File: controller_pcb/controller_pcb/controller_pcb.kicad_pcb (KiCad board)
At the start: 2 copper layers, 34 parts, among them J1 USB_B_Micro, Y1 8MHz

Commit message: initial wiring done
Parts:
- moved C6 3.09 mm to (144.8, 119.9)
- moved C3 2.54 mm to (159.3, 119.4)
- moved C4 2.54 mm to (166.1, 119.4)
- moved C5 2.54 mm to (172.5, 119.4)
- moved C7 2.54 mm to (152.7, 119.4)
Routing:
- net PC9: track 0.00 -> 336.2 mm, vias 0 -> 2
- net PE7: track 0.00 -> 311.0 mm, vias 0 -> 2
- net +3V3: track 0.00 -> 308.3 mm
- net PC8: track 0.00 -> 266.5 mm, vias 0 -> 6
- net PC1: track 0.00 -> 171.4 mm, vias 0 -> 6
- net Y2: track 0.00 -> 131.7 mm, vias 0 -> 2
- net X1: track 0.00 -> 115.4 mm, vias 0 -> 4
- net SEL2: track 0.00 -> 112.7 mm, vias 0 -> 2
- net PD1: track 0.00 -> 94.6 mm, vias 0 -> 2
- net X2: track 0.00 -> 92.3 mm, vias 0 -> 2
- net USB_DP: track 0.00 -> 89.9 mm, vias 0 -> 2
- net PD2: track 0.00 -> 87.5 mm, vias 0 -> 4
- net Y1: track 0.00 -> 79.2 mm, vias 0 -> 4
- net PC11: track 0.00 -> 79.2 mm, vias 0 -> 4
- net PC4: track 0.00 -> 76.5 mm, vias 0 -> 4
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
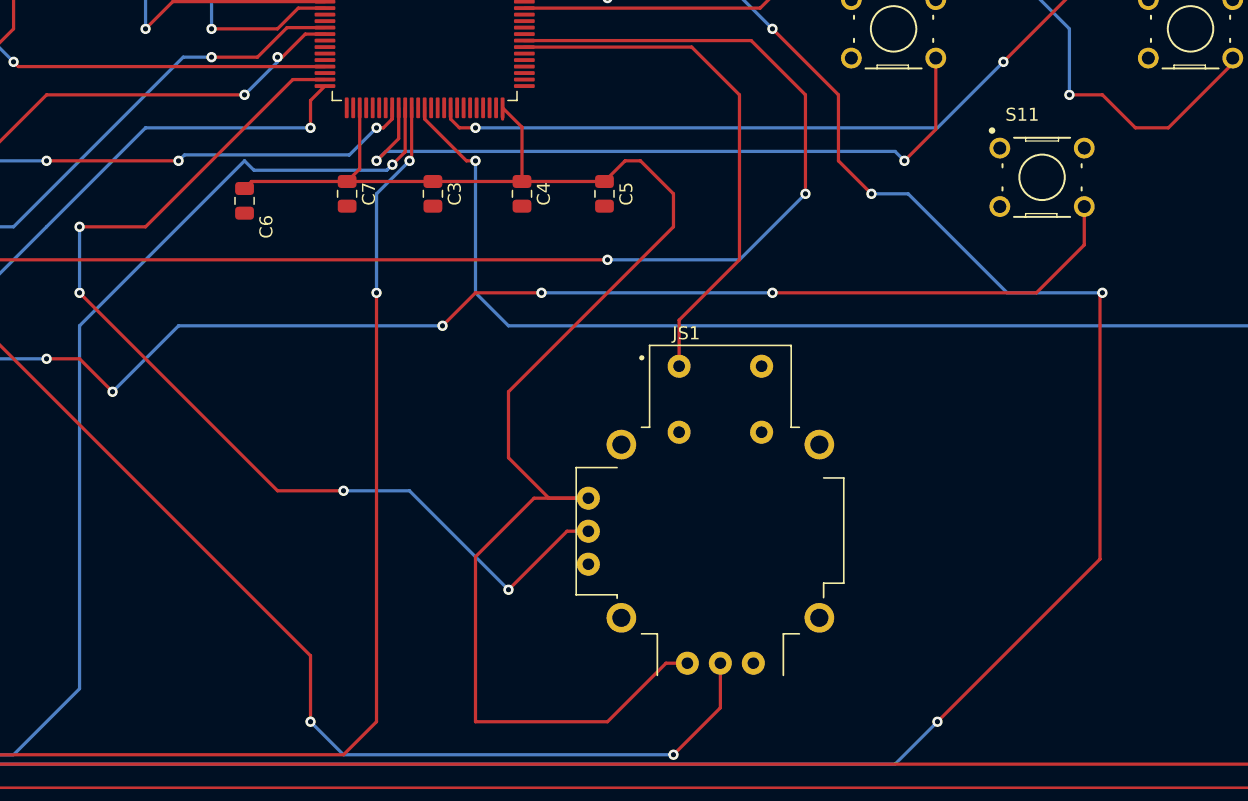
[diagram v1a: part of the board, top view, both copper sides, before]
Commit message: Fixed some right angles
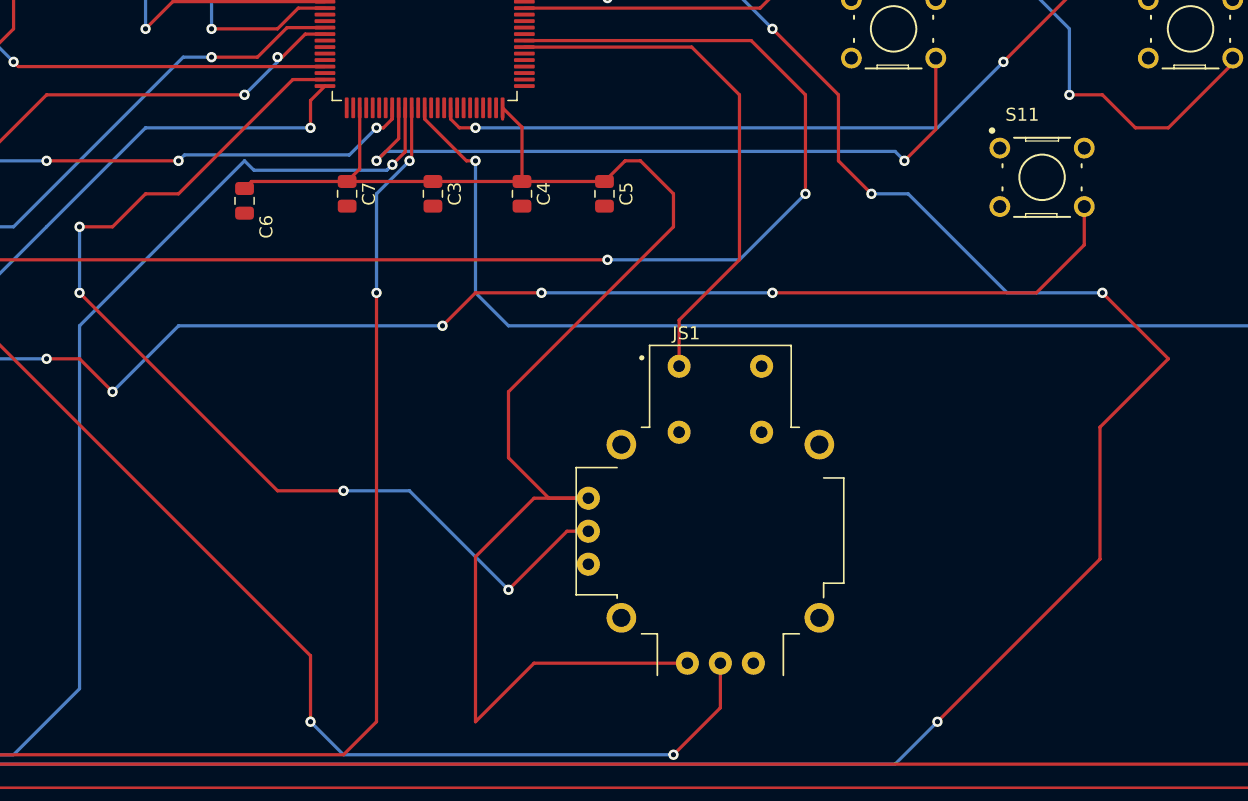
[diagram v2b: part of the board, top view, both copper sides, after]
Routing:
- net PC8: track 266.5 -> 270.7 mm
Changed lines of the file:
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@@
   (segment (start 170.18 55.88) (end 172.72 55.88) (width 0.25) (layer "B.Cu") (net 1))
   (segment (start 157.48 55.88) (end 170.18 55.88) (width 0.25) (layer "B.Cu") (net 1))
+  (segment (start 171.25 142.812846) (end 167.067154 142.812846) (width 0.25) (layer "F.Cu") (net 3))
   (segment (start 105.663999 141.986001) (end 104.775 142.875) (width 0.25) (layer "F.Cu") (net 3))
   (segment (start 159.281 118.43) (end 166.139 118.43) (width 0.25) (layer "F.Cu") (net 3))
@@
   (segment (start 164.646 113.624006) (end 164.646 112.759) (width 0.25) (layer "F.Cu") (net 3))
   (segment (start 166.139 114.252) (end 166.139 118.43) (width 0.25) (layer "F.Cu") (net 3))
-  (segment (start 167.067154 142.812846) (end 162.56 147.32) (width 0.25) (layer "F.Cu") (net 3))
-  (segment (start 172.72 160.02) (end 177.227154 155.512846) (width 0.25) (layer "F.Cu") (net 3))
   (segment (start 165.1 134.62) (end 165.1 139.7) (width 0.25) (layer "F.Cu") (net 3))
   (segment (start 166.139 118.43) (end 172.489 118.43) (width 0.25) (layer "F.Cu") (net 3))
+  (segment (start 167.067154 155.512846) (end 178.87 155.512846) (width 0.25) (layer "F.Cu") (net 3))
+  (segment (start 167.067154 142.812846) (end 162.56 147.32) (width 0.25) (layer "F.Cu") (net 3))
   (segment (start 168.8005 63.307) (end 166.0675 66.04) (width 0.25) (layer "F.Cu") (net 3))
   (segment (start 111.125 155.575) (end 112.395 155.575) (width 0.25) (layer "F.Cu") (net 3))
   (segment (start 165.1 55.88) (end 165.1 60.96) (width 0.25) (layer "F.Cu") (net 3))
-  (segment (start 162.56 147.32) (end 162.56 160.02) (width 0.25) (layer "F.Cu") (net 3))
   (segment (start 177.8 119.38) (end 177.8 121.92) (width 0.25) (layer "F.Cu") (net 3))
   (segment (start 151.77 86.365) (end 149.865 86.365) (width 0.25) (layer "F.Cu") (net 3))
@@
   (segment (start 153.543 69.977) (end 157.358 69.977) (width 0.25) (layer "F.Cu") (net 3))
   (segment (start 161.295 66.04) (end 157.358 69.977) (width 0.25) (layer "F.Cu") (net 3))
+  (segment (start 162.56 160.02) (end 167.067154 155.512846) (width 0.25) (layer "F.Cu") (net 3))
   (segment (start 152.677 118.43) (end 159.281 118.43) (width 0.25) (layer "F.Cu") (net 3))
   (segment (start 177.8 121.92) (end 165.1 134.62) (width 0.25) (layer "F.Cu") (net 3))
@@
   (segment (start 165.1 139.7) (end 168.212846 142.812846) (width 0.25) (layer "F.Cu") (net 3))
   (segment (start 152.646 97.409) (end 151.77 96.533) (width 0.25) (layer "F.Cu") (net 3))
-  (segment (start 171.25 142.812846) (end 167.067154 142.812846) (width 0.25) (layer "F.Cu") (net 3))
+  (segment (start 162.56 147.32) (end 162.56 160.02) (width 0.25) (layer "F.Cu") (net 3))
   (segment (start 168.999 49.276) (end 168.999 51.981) (width 0.25) (layer "F.Cu") (net 3))
   (segment (start 147.32 76.2) (end 153.543 69.977) (width 0.25) (layer "F.Cu") (net 3))
@@
   (segment (start 124.945 97.79) (end 128.739 101.584) (width 0.25) (layer "F.Cu") (net 3))
   (segment (start 167.447 63.307) (end 168.8005 63.307) (width 0.25) (layer "F.Cu") (net 3))
-  (segment (start 162.56 160.02) (end 172.72 160.02) (width 0.25) (layer "F.Cu") (net 3))
   (segment (start 147.32 83.82) (end 147.32 76.2) (width 0.25) (layer "F.Cu") (net 3))
   (segment (start 128.739 101.584) (end 127 103.323) (width 0.25) (layer "F.Cu") (net 3))
-  (segment (start 177.227154 155.512846) (end 178.87 155.512846) (width 0.25) (layer "F.Cu") (net 3))
   (segment (start 105.663999 128.016001) (end 105.663999 141.986001) (width 0.25) (layer "F.Cu") (net 3))
   (segment (start 96.52 147.32) (end 96.52 154.94) (width 0.25) (layer "F.Cu") (net 3))
@@
   (segment (start 147.32 142.24) (end 152.4 142.24) (width 0.25) (layer "F.Cu") (net 28))
   (segment (start 150.971 110.584) (end 148.496 110.584) (width 0.25) (layer "F.Cu") (net 28))
-  (segment (start 148.496 110.584) (end 137.16 121.92) (width 0.25) (layer "F.Cu") (net 28))
+  (segment (start 134.62 121.92) (end 132.08 121.92) (width 0.25) (layer "F.Cu") (net 28))
   (segment (start 132.08 127) (end 147.32 142.24) (width 0.25) (layer "F.Cu") (net 28))
+  (segment (start 148.496 110.584) (end 139.7 119.38) (width 0.25) (layer "F.Cu") (net 28))
+  (segment (start 139.7 119.38) (end 137.16 119.38) (width 0.25) (layer "F.Cu") (net 28))
+  (segment (start 137.16 119.38) (end 134.62 121.92) (width 0.25) (layer "F.Cu") (net 28))
   (segment (start 169.607154 145.352846) (end 171.25 145.352846) (width 0.25) (layer "F.Cu") (net 28))
-  (segment (start 137.16 121.92) (end 132.08 121.92) (width 0.25) (layer "F.Cu") (net 28))
   (via (at 165.1 149.86) (size 0.8) (drill 0.4) (layers "F.Cu" "B.Cu") (net 28))
   (via (at 132.08 121.92) (size 0.8) (drill 0.4) (layers "F.Cu" "B.Cu") (net 28))
@@
   (segment (start 187.96 98.582846) (end 187.96 101.6) (width 0.25) (layer "F.Cu") (net 64))
   (segment (start 187.96 101.6) (end 184.476 105.084) (width 0.25) (layer "F.Cu") (net 64))
-  (segment (start 210.633802 127.186198) (end 210.82 127) (width 0.25) (layer "F.Cu") (net 66))
+  (segment (start 210.633802 147.506198) (end 210.633802 137.346198) (width 0.25) (layer "F.Cu") (net 66))
   (segment (start 172.72 104.3085) (end 172.4955 104.084) (width 0.25) (layer "F.Cu") (net 66))
+  (segment (start 210.633802 137.346198) (end 215.9 132.08) (width 0.25) (layer "F.Cu") (net 66))
   (segment (start 198.12 160.02) (end 210.633802 147.506198) (width 0.25) (layer "F.Cu") (net 66))
-  (segment (start 210.633802 147.506198) (end 210.633802 127.186198) (width 0.25) (layer "F.Cu") (net 66))
   (segment (start 193.04 119.38) (end 190.5 116.84) (width 0.25) (layer "F.Cu") (net 66))
   (segment (start 172.4955 104.084) (end 166.321 104.084) (width 0.25) (layer "F.Cu") (net 66))
   (segment (start 80.72 156.92) (end 81.28 157.48) (width 0.25) (layer "F.Cu") (net 66))
+  (segment (start 215.9 132.08) (end 210.82 127) (width 0.25) (layer "F.Cu") (net 66))
   (segment (start 190.5 111.76) (end 185.42 106.68) (width 0.25) (layer "F.Cu") (net 66))
   (segment (start 190.5 116.84) (end 190.5 111.76) (width 0.25) (layer "F.Cu") (net 66))

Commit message: almost done w traces
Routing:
- net +3V3: track 308.3 -> 364.3 mm
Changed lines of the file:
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@@
   (segment (start 157.48 55.88) (end 170.18 55.88) (width 0.25) (layer "B.Cu") (net 1))
   (segment (start 171.25 142.812846) (end 167.067154 142.812846) (width 0.25) (layer "F.Cu") (net 3))
+  (segment (start 153.646 112.759) (end 153.646 111.893315) (width 0.25) (layer "F.Cu") (net 3))
   (segment (start 105.663999 141.986001) (end 104.775 142.875) (width 0.25) (layer "F.Cu") (net 3))
   (segment (start 159.281 118.43) (end 166.139 118.43) (width 0.25) (layer "F.Cu") (net 3))
   (segment (start 100.965 142.875) (end 96.52 147.32) (width 0.25) (layer "F.Cu") (net 3))
+  (segment (start 150.971 108.084) (end 151.836685 108.084) (width 0.25) (layer "F.Cu") (net 3))
+  (segment (start 153.396342 103.143658) (end 154.666342 104.413658) (width 0.25) (layer "F.Cu") (net 3))
   (segment (start 96.52 154.94) (end 101.6 160.02) (width 0.25) (layer "F.Cu") (net 3))
   (segment (start 175.26 116.84) (end 177.8 119.38) (width 0.25) (layer "F.Cu") (net 3))
   (segment (start 164.646 113.624006) (end 164.646 112.759) (width 0.25) (layer "F.Cu") (net 3))
   (segment (start 166.139 114.252) (end 166.139 118.43) (width 0.25) (layer "F.Cu") (net 3))
+  (segment (start 160.709657 104.829657) (end 162.56 102.979315) (width 0.25) (layer "F.Cu") (net 3))
+  (segment (start 152.646 102.393316) (end 153.396342 103.143658) (width 0.25) (layer "F.Cu") (net 3))
   (segment (start 165.1 134.62) (end 165.1 139.7) (width 0.25) (layer "F.Cu") (net 3))
+  (segment (start 153.646 111.893315) (end 156.899657 108.639657) (width 0.25) (layer "F.Cu") (net 3))
   (segment (start 166.139 118.43) (end 172.489 118.43) (width 0.25) (layer "F.Cu") (net 3))
   (segment (start 167.067154 155.512846) (end 178.87 155.512846) (width 0.25) (layer "F.Cu") (net 3))
   (segment (start 167.067154 142.812846) (end 162.56 147.32) (width 0.25) (layer "F.Cu") (net 3))
+  (segment (start 156.899657 108.639657) (end 158.169657 107.369657) (width 0.25) (layer "F.Cu") (net 3))
   (segment (start 168.8005 63.307) (end 166.0675 66.04) (width 0.25) (layer "F.Cu") (net 3))
   (segment (start 111.125 155.575) (end 112.395 155.575) (width 0.25) (layer "F.Cu") (net 3))
+  (segment (start 154.666342 104.413658) (end 155.082342 104.829657) (width 0.25) (layer "F.Cu") (net 3))
   (segment (start 165.1 55.88) (end 165.1 60.96) (width 0.25) (layer "F.Cu") (net 3))
   (segment (start 177.8 119.38) (end 177.8 121.92) (width 0.25) (layer "F.Cu") (net 3))
   (segment (start 151.77 86.365) (end 149.865 86.365) (width 0.25) (layer "F.Cu") (net 3))
+  (segment (start 150.971 104.084) (end 154.336684 104.084) (width 0.25) (layer "F.Cu") (net 3))
+  (segment (start 152.646 97.409) (end 152.646 102.393316) (width 0.25) (layer "F.Cu") (net 3))
   (segment (start 149.865 86.365) (end 147.32 83.82) (width 0.25) (layer "F.Cu") (net 3))
   (segment (start 153.543 69.977) (end 157.358 69.977) (width 0.25) (layer "F.Cu") (net 3))
@@
   (segment (start 152.677 118.43) (end 159.281 118.43) (width 0.25) (layer "F.Cu") (net 3))
   (segment (start 177.8 121.92) (end 165.1 134.62) (width 0.25) (layer "F.Cu") (net 3))
+  (segment (start 155.082342 104.829657) (end 160.709657 104.829657) (width 0.25) (layer "F.Cu") (net 3))
   (segment (start 168.212846 142.812846) (end 171.25 142.812846) (width 0.25) (layer "F.Cu") (net 3))
   (segment (start 164.646 112.759) (end 166.139 114.252) (width 0.25) (layer "F.Cu") (net 3))
@@
   (segment (start 166.0675 66.04) (end 161.295 66.04) (width 0.25) (layer "F.Cu") (net 3))
   (segment (start 165.1 139.7) (end 168.212846 142.812846) (width 0.25) (layer "F.Cu") (net 3))
+  (segment (start 150.971 101.584) (end 151.836685 101.584) (width 0.25) (layer "F.Cu") (net 3))
   (segment (start 152.646 97.409) (end 151.77 96.533) (width 0.25) (layer "F.Cu") (net 3))
+  (segment (start 162.56 101.6) (end 165.076 99.084) (width 0.25) (layer "F.Cu") (net 3))
   (segment (start 162.56 147.32) (end 162.56 160.02) (width 0.25) (layer "F.Cu") (net 3))
   (segment (start 168.999 49.276) (end 168.999 51.981) (width 0.25) (layer "F.Cu") (net 3))
   (segment (start 147.32 76.2) (end 153.543 69.977) (width 0.25) (layer "F.Cu") (net 3))
   (segment (start 101.6 160.02) (end 106.68 160.02) (width 0.25) (layer "F.Cu") (net 3))
+  (segment (start 154.336684 104.084) (end 154.666342 104.413658) (width 0.25) (layer "F.Cu") (net 3))
   (segment (start 152.677 118.43) (end 153.646 117.461) (width 0.25) (layer "F.Cu") (net 3))
   (segment (start 128.739 101.584) (end 150.971 101.584) (width 0.25) (layer "F.Cu") (net 3))
@@
   (segment (start 127 106.68) (end 105.663999 128.016001) (width 0.25) (layer "F.Cu") (net 3))
   (segment (start 124.945 97.79) (end 128.739 101.584) (width 0.25) (layer "F.Cu") (net 3))
+  (segment (start 151.836685 101.584) (end 153.396342 103.143658) (width 0.25) (layer "F.Cu") (net 3))
+  (segment (start 162.56 102.979315) (end 162.56 101.6) (width 0.25) (layer "F.Cu") (net 3))
   (segment (start 167.447 63.307) (end 168.8005 63.307) (width 0.25) (layer "F.Cu") (net 3))
   (segment (start 147.32 83.82) (end 147.32 76.2) (width 0.25) (layer "F.Cu") (net 3))
+  (segment (start 151.836685 108.084) (end 152.392342 108.639657) (width 0.25) (layer "F.Cu") (net 3))
   (segment (start 128.739 101.584) (end 127 103.323) (width 0.25) (layer "F.Cu") (net 3))
+  (segment (start 165.076 99.084) (end 166.321 99.084) (width 0.25) (layer "F.Cu") (net 3))
   (segment (start 105.663999 128.016001) (end 105.663999 141.986001) (width 0.25) (layer "F.Cu") (net 3))
   (segment (start 96.52 147.32) (end 96.52 154.94) (width 0.25) (layer "F.Cu") (net 3))
+  (segment (start 158.169657 107.369657) (end 160.709657 104.829657) (width 0.25) (layer "F.Cu") (net 3))
+  (segment (start 152.392342 108.639657) (end 156.899657 108.639657) (width 0.25) (layer "F.Cu") (net 3))
   (segment (start 174.079 116.84) (end 175.26 116.84) (width 0.25) (layer "F.Cu") (net 3))
+  (segment (start 164.646 112.759) (end 164.646 111.893315) (width 0.25) (layer "F.Cu") (net 3))
   (segment (start 127 103.323) (end 127 106.68) (width 0.25) (layer "F.Cu") (net 3))
   (segment (start 106.68 160.02) (end 111.125 155.575) (width 0.25) (layer "F.Cu") (net 3))
+  (segment (start 164.646 111.893315) (end 160.122342 107.369657) (width 0.25) (layer "F.Cu") (net 3))
   (segment (start 165.1 60.96) (end 167.447 63.307) (width 0.25) (layer "F.Cu") (net 3))
   (segment (start 153.646 117.461) (end 153.646 112.759) (width 0.25) (layer "F.Cu") (net 3))
+  (segment (start 160.122342 107.369657) (end 158.169657 107.369657) (width 0.25) (layer "F.Cu") (net 3))
   (segment (start 151.77 96.533) (end 151.77 86.365) (width 0.25) (layer "F.Cu") (net 3))
   (segment (start 104.775 142.875) (end 100.965 142.875) (width 0.25) (layer "F.Cu") (net 3))
